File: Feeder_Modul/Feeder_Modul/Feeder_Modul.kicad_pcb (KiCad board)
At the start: 2 copper layers, 156.6 x 125.2 mm, 102 parts, among them J1 Conn_02x01, J101 Conn_02x01, J102 Conn_01x06_Male, J103 Conn_02x01, J104 Conn_02x01, J105 Conn_02x01, J106 WE_629104190121, J107 Conn_02x07_Odd_Even, J108 Conn_02x01, J109 Conn_02x01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

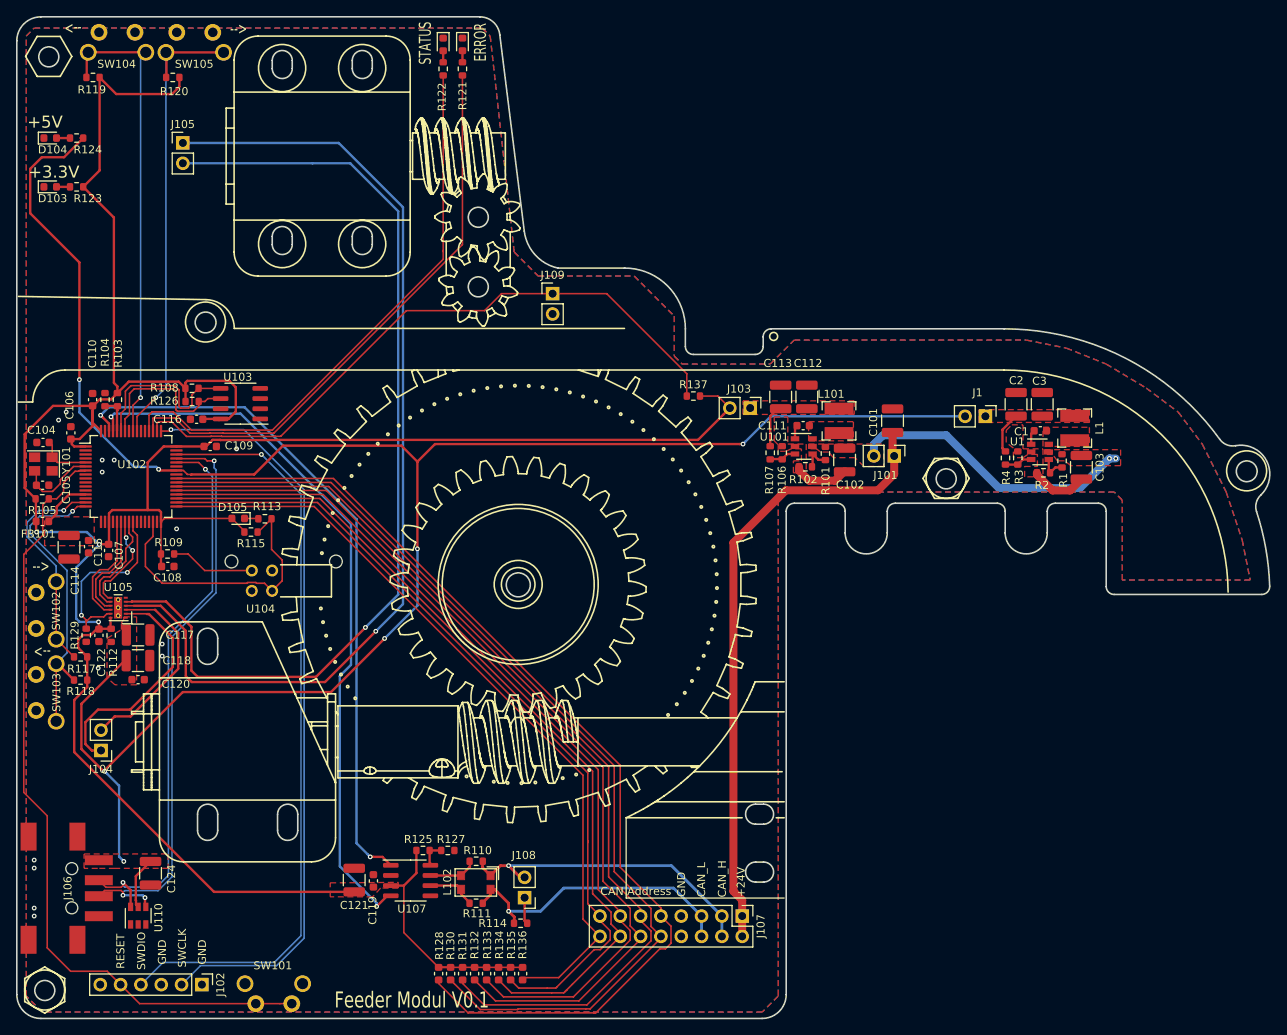
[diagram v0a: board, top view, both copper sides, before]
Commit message: Fiducials auf allen Boards hinzugefügt
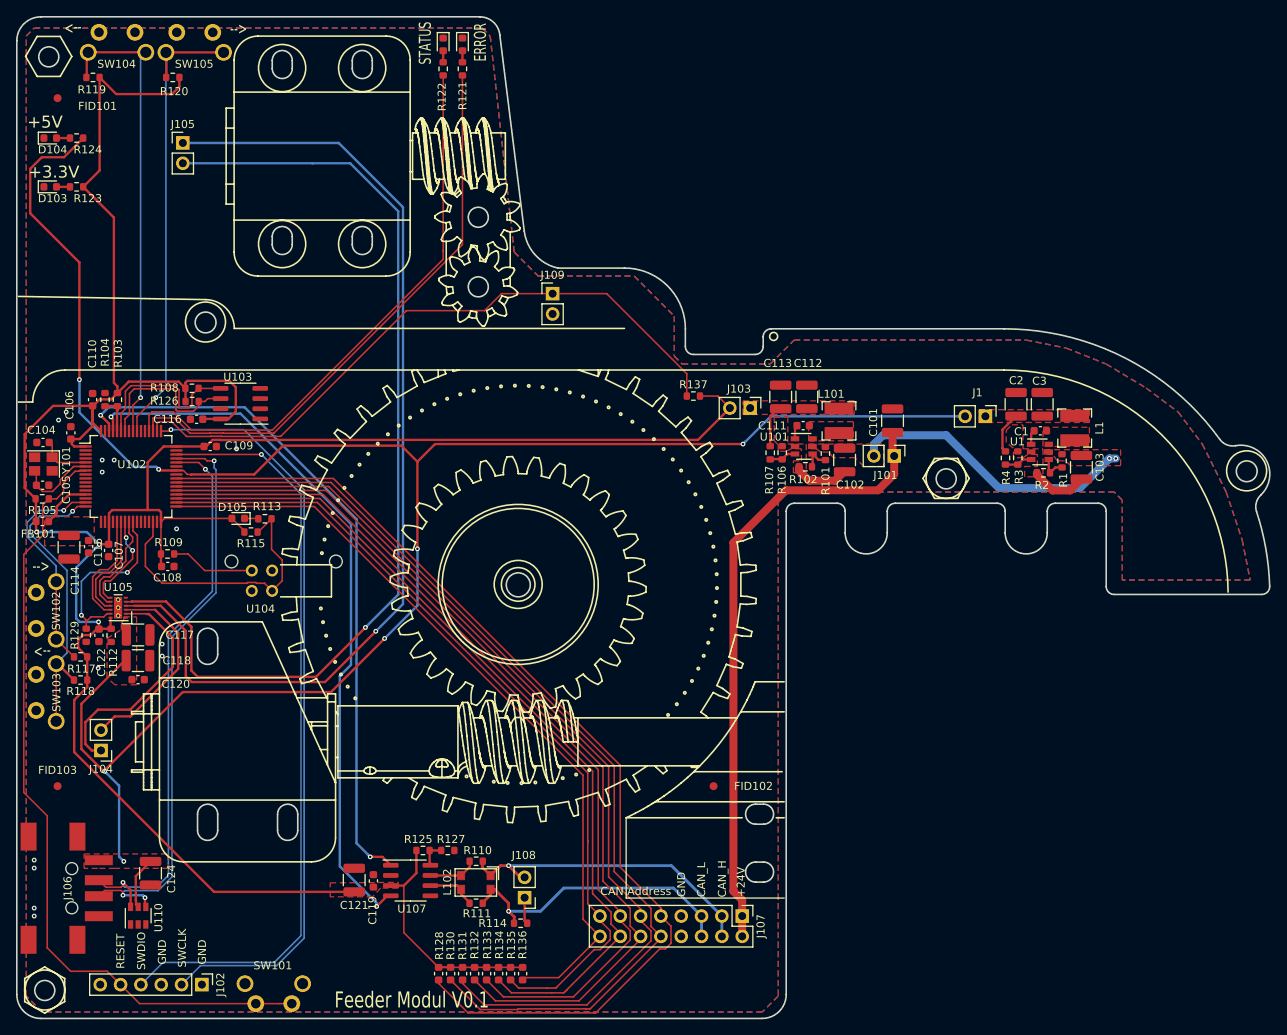
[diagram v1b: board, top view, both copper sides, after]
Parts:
- added FID101: Fiducial, Fiducial:Fiducial_1mm_Mask2mm, F.Cu at (68.9, 45.8)
- added FID102: Fiducial, Fiducial:Fiducial_1mm_Mask2mm, F.Cu at (150.9, 131.8)
- added FID103: Fiducial, Fiducial:Fiducial_1mm_Mask2mm, F.Cu at (68.9, 131.8)

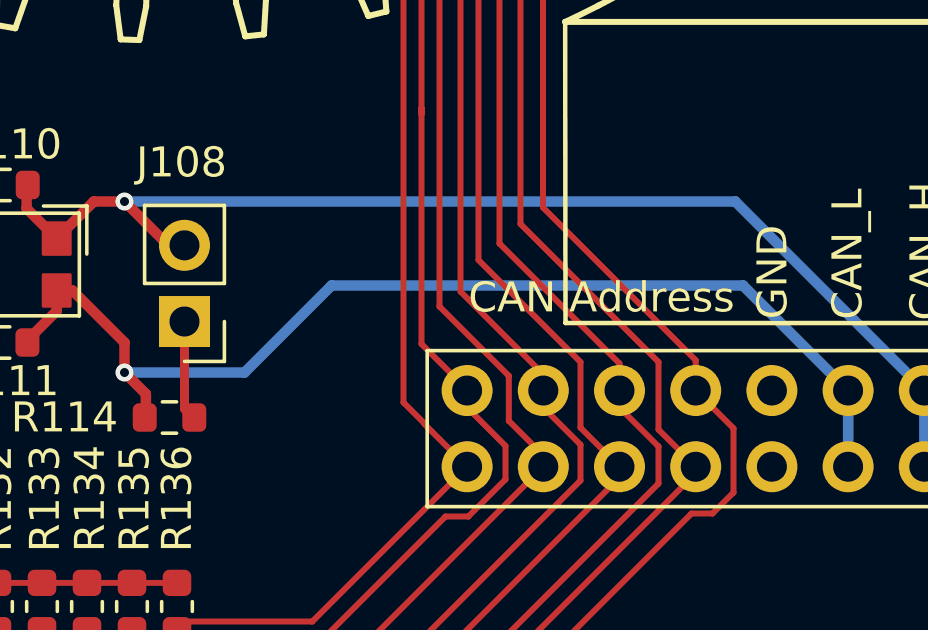
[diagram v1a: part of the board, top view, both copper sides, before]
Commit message: ESD Protection überarbeitet, aber noch nicht fertig
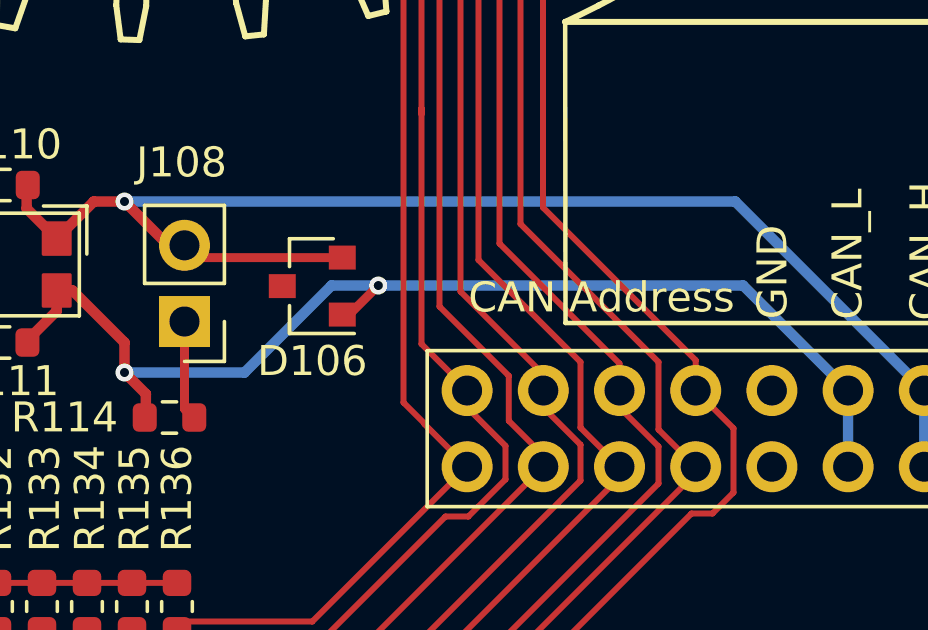
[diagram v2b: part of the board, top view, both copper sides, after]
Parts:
- added D106: SM24CANA-02HTG, Package_TO_SOT_SMD:SOT-23, F.Cu at (131.6, 144.5)
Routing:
- net /CAN1_H: track 39.4 -> 44.8 mm
- net /CAN1_L: track 37.3 -> 38.9 mm, vias 1 -> 2

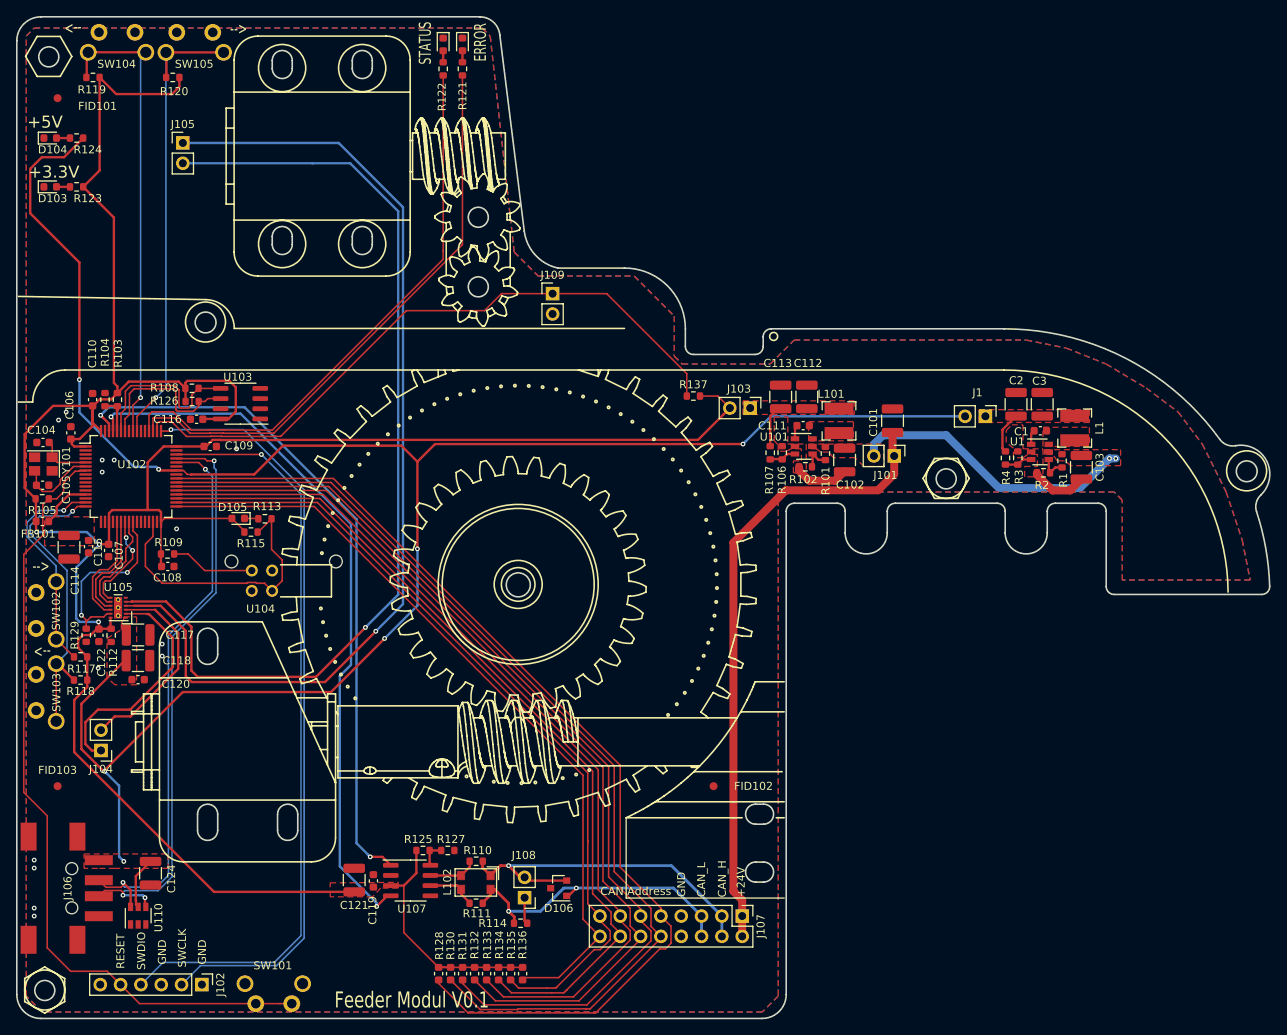
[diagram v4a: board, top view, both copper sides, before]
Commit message: Kleine Bugs im Feeder behoben, Löcher für Lagerhalter hinzugefügt
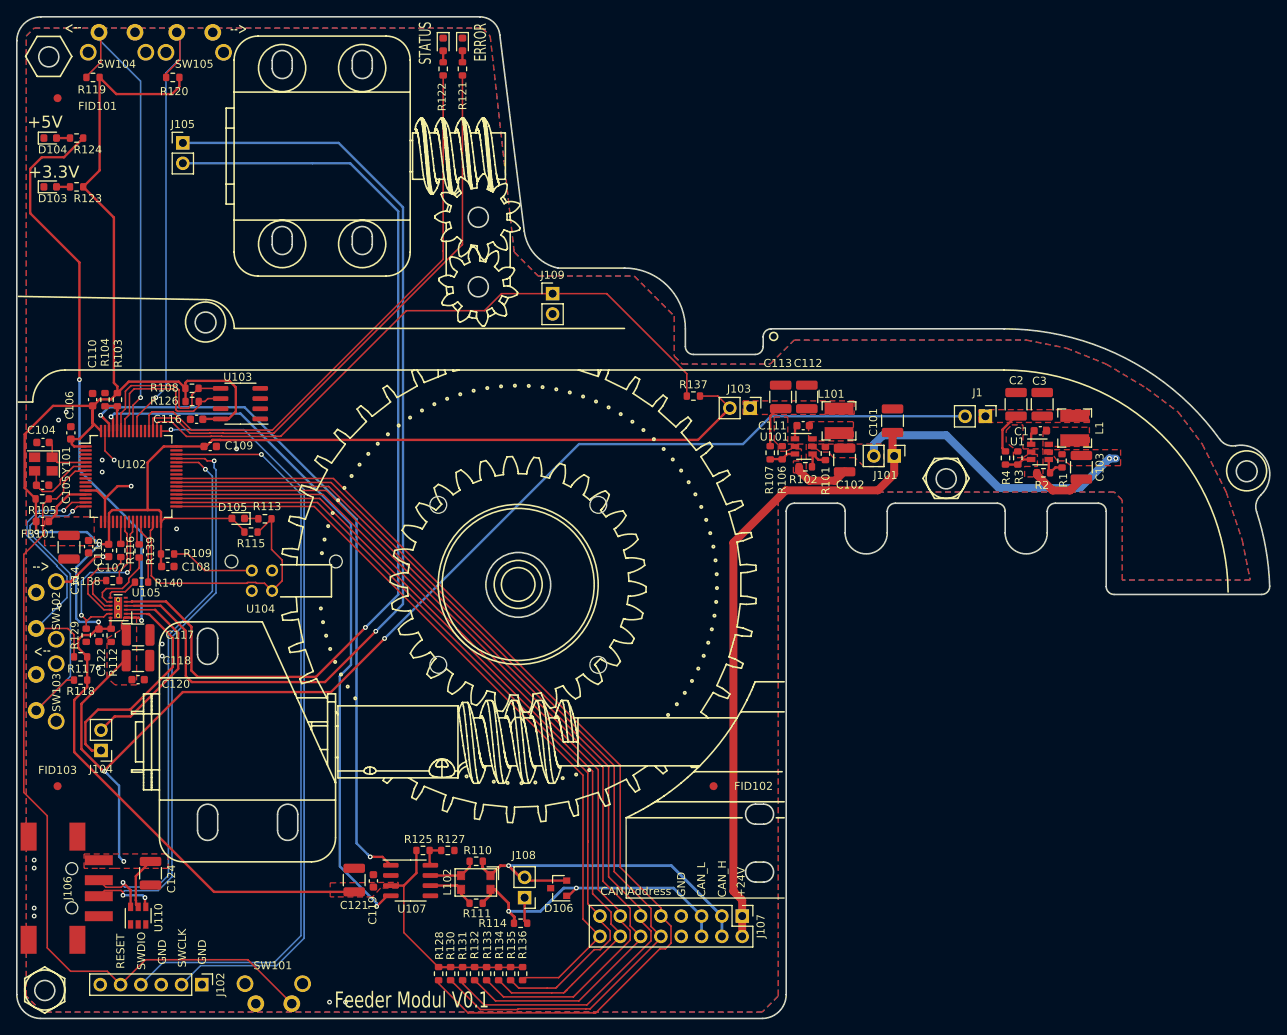
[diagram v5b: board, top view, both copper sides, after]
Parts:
- added R116: 1k, Resistor_SMD:R_0603_1608Metric, F.Cu at (76.8, 102.3)
- added R138: 1k, Resistor_SMD:R_0603_1608Metric, F.Cu at (75.8, 106.1)
- added R139: 1k, Resistor_SMD:R_0603_1608Metric, F.Cu at (79.1, 102.4)
- added R140: 1k, Resistor_SMD:R_0603_1608Metric, F.Cu at (79.4, 106.3)
- R109: value 1k -> 120R
- Y101: value 48MHz -> 8MHz
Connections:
- SW102 pad 1: /BTN_TBACK -> GND
- SW102 pad 2: GND -> /BTN_TBACK
- SW103 pad 1: /BTN_TFOR -> GND
- SW103 pad 2: GND -> /BTN_TFOR
- SW104 pad 1: /BTN_SBACK -> GND
- SW104 pad 2: GND -> /BTN_SBACK
- SW105 pad 1: /BTN_SFOR -> GND
- SW105 pad 2: GND -> /BTN_SFOR
- U102 pad 21: /DIR_A -> (no net)
- U102 pad 24: /DIR_B -> (no net)
- U102 pad 26: (no net) -> /TIM3_CH3
- U102 pad 27: (no net) -> /TIM3_CH4
- U102 pad 42: +5V -> (no net)
- U105 pad 10: /DIR_A -> /PWM_A
- U105 pad 7: /PA7 -> /PWM_D
- U105 pad 8: /DIR_B -> /PWM_C
- U105 pad 9: /PA6 -> /PWM_B
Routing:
- net +5V: track 262.2 -> 235.2 mm, vias 7 -> 5
- net GND: track 14.4 -> 36.9 mm, vias 14 -> 18
- net /DIR_A: track 14.3 -> 0.00 mm
- net /DIR_B: track 13.1 -> 0.00 mm
- net /PWM_A: track 0.00 -> 11.2 mm
- net /PA6: track 13.5 -> 2.76 mm
- net /PWM_C: track 0.00 -> 9.29 mm
- net /TIM3_CH4: track 0.00 -> 7.91 mm
- net /PWM_B: track 0.00 -> 6.00 mm
- net /BTN_TBACK: track 27.6 -> 33.1 mm, vias 1 -> 2
- net /PA7: track 12.3 -> 7.85 mm, vias 2 -> 0
- net /PWM_D: track 0.00 -> 4.21 mm
- net /BTN_TFOR: track 38.2 -> 41.2 mm
- net /TIM3_CH3: track 0.00 -> 2.92 mm
- net /NRST: track 98.9 -> 101.4 mm
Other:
- outline, holes or cut-outs redrawn
